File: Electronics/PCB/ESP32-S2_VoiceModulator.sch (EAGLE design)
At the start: 17 parts, among them IC1 ESP32-S2, IC2 AT25SF041-SSHD-B, J1 0532610671, Y1 FA-20H_40.0000MF15Z-AC3

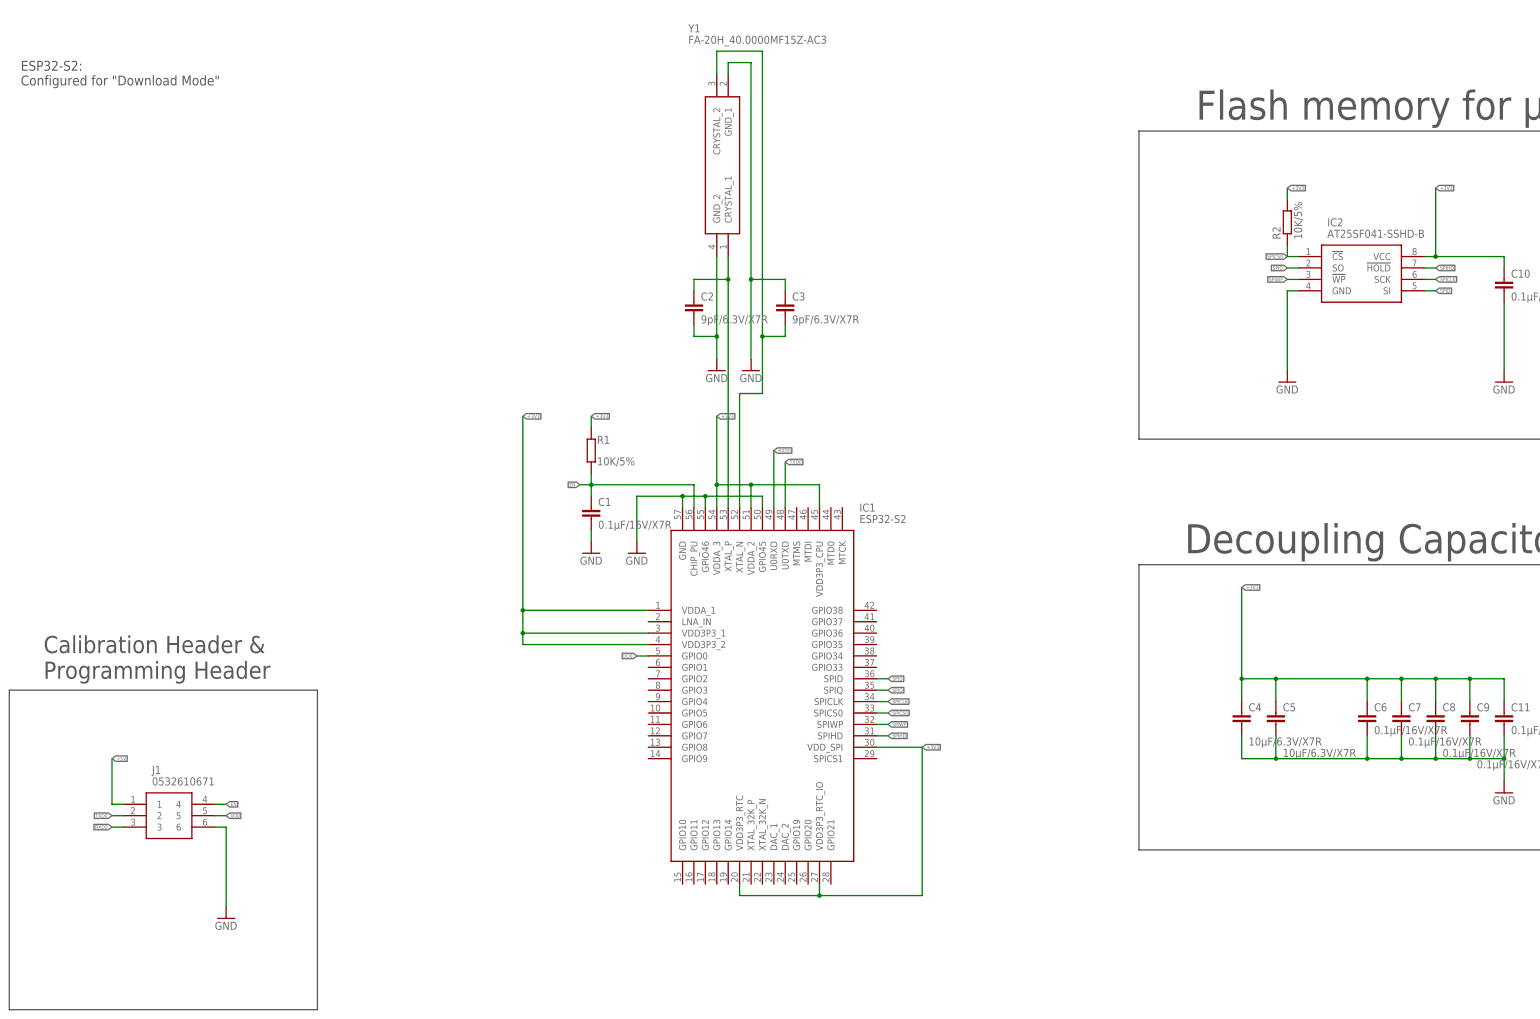
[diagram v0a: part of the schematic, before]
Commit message: CHanged labelign for VCC/ power
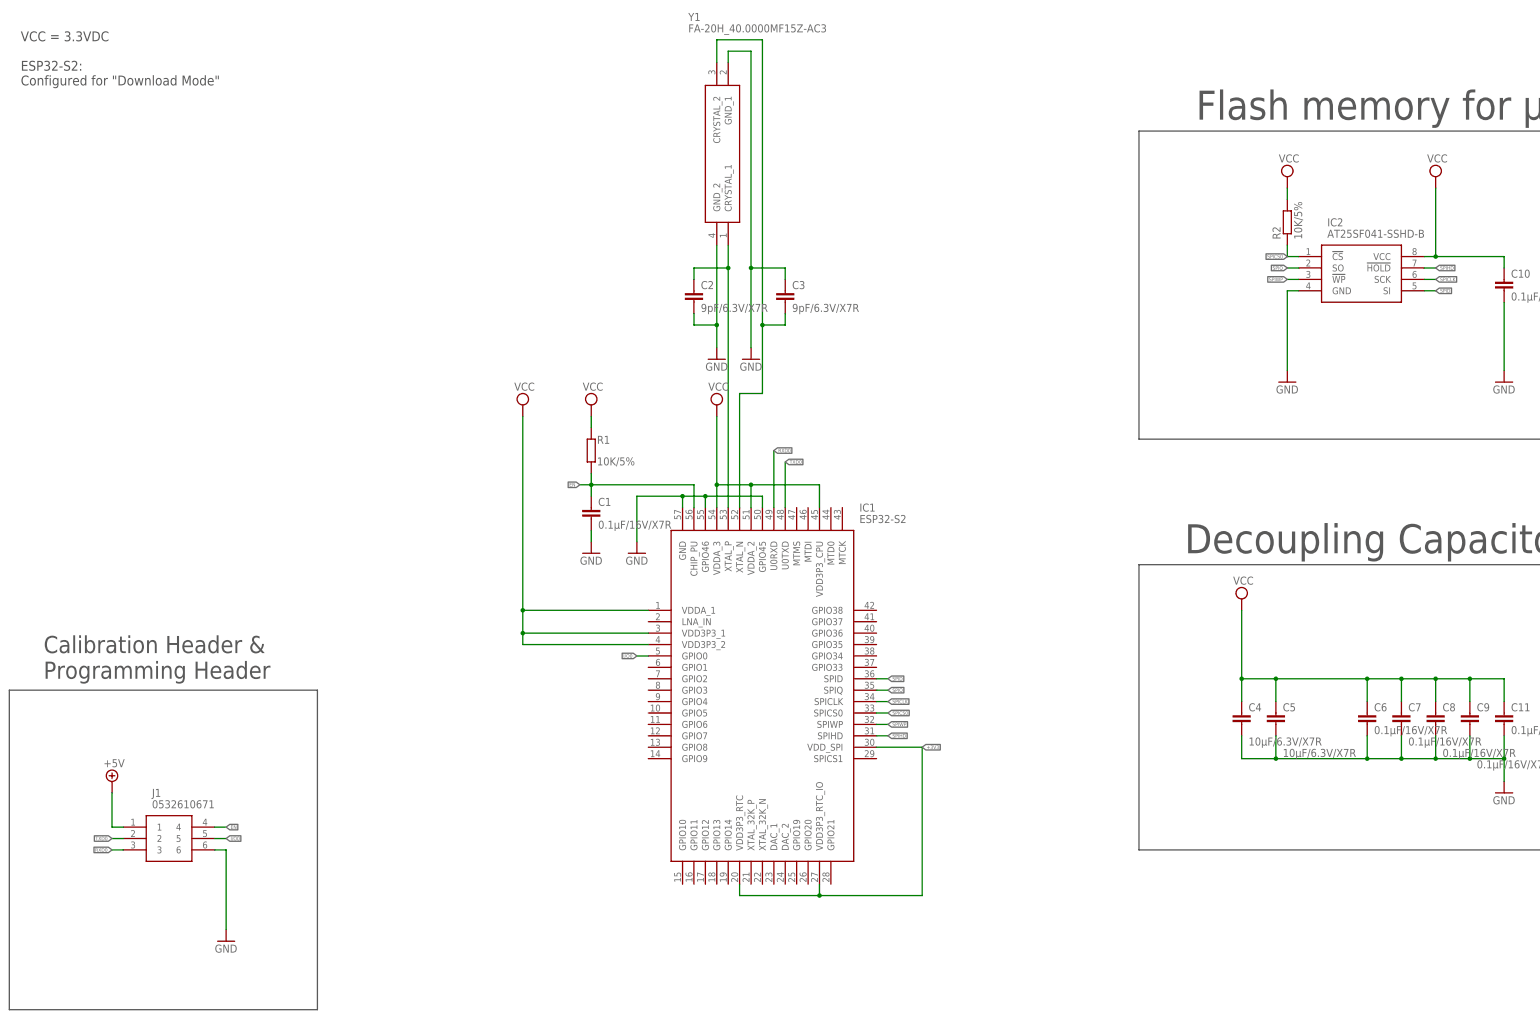
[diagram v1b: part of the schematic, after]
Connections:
- new net VCC: C10.1, C11.1, C4.1, C5.1, C6.1, C7.1, C8.1, C9.1, IC1.VDD3P3_1, IC1.VDD3P3_2, IC1.VDD3P3_CPU, IC1.VDDA_1, IC1.VDDA_2, IC1.VDDA_3, IC2.VCC, R1.2, R2.2
- net +3V3: no longer C10.1, C11.1, C4.1, C5.1, C6.1, C7.1, C8.1, C9.1, IC1.VDD3P3_1, IC1.VDD3P3_2, IC1.VDD3P3_CPU, IC1.VDDA_1, IC1.VDDA_2, IC1.VDDA_3, IC2.VCC, R1.2, R2.2
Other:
- note added: "VCC = 3.3VDC ESP32-S2: Configured for "Download Mode""
- note removed: "ESP32-S2: Configured for "Download Mode""
- moved on the sheet: C2, C3, J1, Y1

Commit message: Added schematic drawing for the microphone emulation and PCB microphone adjustment.
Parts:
- added C12, C13, C15: 1uF/6.3V, resistor:C-EUC0603
- added C14: 0.1µF/16V, rcl:C-EUC0402
- added J2, J3: (no value), VoiceModulator:SJ2-35364B-SMT-TR
- added MK1: WMM7022AT0, VoiceModulator:WMM7022AT0
- added OP1: MCP6001T-I/OT, VoiceModulator:MCP6001T-I/OT
- added Q1: CPH3910, VoiceModulator:CPH3910
- added R10, R9: 1K, resistor:R-EU_R0603
- added R11: 70k, resistor:R-EU_R0603
- added R12, R13, R8: 100K, resistor:R-EU_R0603
- added R3, R5, R6, R7: 10K, resistor:R-EU_R0603
- added R4: 100R, resistor:R-EU_R0603
- C1, C10, C11, C6, C7, C8, C9: value 0.1µF/16V/X7R -> 0.1µF/16V
- C2, C3: value 9pF/6.3V/X7R -> 9pF/6.3V
- C4, C5: value 10µF/6.3V/X7R -> 10µF/6.3V
- R1, R2: value 10K/5% -> 10K
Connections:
- new net AGND: J2.4, J3.4, Q1.S, R5.2
- new net AUDIO_LEFT: J2.2, J3.2
- new net AUDIO_RIGHT: J2.3, J3.3
- new net DAC_OUTPUT: R3.2
- new net HEADPHONE_SWITCH: J2.10
- new net MICROPHONE_HEADSET: J2.1
- new net MICROPHONE_OUT: J3.1, R6.1, R7.2
- new net N$1: C12.2, Q1.G, R5.1
- new net N$2: C12.1, R3.1, R4.2
- new net N$3: C13.2, OP1.V+, R8.1, R9.2
- new net N$4: C13.1, MK1.OUT
- new net N$5: Q1.D, R6.2, R7.1
- new net N$6: OP1.V-, R10.2, R11.2
- new net N$7: C15.1, OP1.VOUT, R11.1
- new net PCB-MICROPHONE_OUTPUT: C15.2, R12.2, R13.1
- new net PHONE_SWITCH: J3.10
- net +5V: now also OP1.VDD
- net GND: now also C14.2, MK1.GND, OP1.VSS, R10.1, R12.1, R4.1, R9.1
- net VCC: now also C14.1, MK1.VDD, R13.2, R8.2
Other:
- note added: "Check if grounding is correct"
- note added: "Headphones"
- note added: "PCB Microphone adjustment"
- note added: "Phone"

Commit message: Added DC/DC
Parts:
- added C16, C17: 1uF/6.3V, resistor:C-EUC0603
- added IC3: MIC5504-3.3YM5-TR, VoiceModulator:MIC5504-3.3YM5-TR
- J2, J3: value (none) -> SJ2-35364B-SMT-TR
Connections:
- net +5V: now also C16.1, IC3.EN, IC3.VIN
- net GND: now also C16.2, C17.2, IC3.GND
- net VCC: now also C17.1, IC3.VOUT
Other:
- note added: "<--- So lonely in a vast empty space :("
- note added: "Microphone emulation"
- note added: "ToDo: Replace ESP32-S2 symbol with functional pinout"

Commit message: Minor changes to schematic
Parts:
- removed J1: 0532610671, SamacSys_Parts:0532610671
- added C18: 0.1µF/16V, resistor:C-EUC0603
- added C19: 0.1µF/16V, rcl:C-EUC0402
- added C20: 1uF/6.3V, resistor:C-EUC0603
- added C21: 10µF/6.3V, rcl:C-EUC0603
- added J4: 10118192-0002LF, VoiceModulator:10118192-0002LF
- added OP2: MCP6001T-I/OT, VoiceModulator:MCP6001T-I/OT
- added R14, R18, R19, R20: 100K, resistor:R-EU_R0603
- added R15, R16: 1K, resistor:R-EU_R0603
- added R17: 70k, resistor:R-EU_R0603
- added TAG_CONNECT_ICSP_HEADER: TAG-CONNECT_PADS, TAG-CONNECT_PADS-lbr:TAG-CONNECT_PADS
- J2: SPICEPREFIX (none) -> X
- R3: value 10K -> 100K
- R4: value 100R -> 1k
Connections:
- removed net AGND: J2.4, J3.4, Q1.S, R5.2
- new net D+: IC1.GPIO19, J4.3
- new net D-: IC1.GPIO20, J4.2
- new net EXTERNAL-MICROPHONE_OUTPUT: C20.2, R18.2, R19.1
- new net ID: J4.4
- new net N$10: OP2.V-, R16.2, R17.2
- new net N$11: C20.1, OP2.VOUT, R17.1
- new net N$9: C18.2, OP2.V+, R14.1, R15.2
- net +5V: now also C21.1, J4.1, OP2.VDD, TAG_CONNECT_ICSP_HEADER.MISO; no longer J1.1
- net EN: now also TAG_CONNECT_ICSP_HEADER.VCC; no longer J1.4
- net GND: now also C19.2, C21.2, J2.4, J3.4, J4.5, OP2.VSS, Q1.S, R15.1, R16.1, R18.1, R5.2, TAG_CONNECT_ICSP_HEADER.GND; no longer J1.6
- net I/O0: now also TAG_CONNECT_ICSP_HEADER.MOSI; no longer J1.5
- net MICROPHONE_HEADSET: now also C18.1, C19.1, R20.1
- net RXD0: now also TAG_CONNECT_ICSP_HEADER.RST; no longer J1.3
- net TXD0: now also TAG_CONNECT_ICSP_HEADER.SCK; no longer J1.2
- net VCC: now also R14.2, R19.2, R20.2
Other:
- note added: "External Microphone adjustment"
- note removed: "Check if grounding is correct"

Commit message: Minor changes
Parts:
- added R21, R22, R23, R24: 10K, resistor:R-EU_R0603
- added S1, S2, S3, S4: PTS647SK70SMTR2LFS, VoiceModulator:PTS647SK70SMTR2LFS
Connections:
- new net SW_1: R21.2, S1.2
- new net SW_2: R22.2, S2.2
- new net SW_3: R23.2, S3.2
- new net SW_4: R24.2, S4.2
- net GND: now also S1.1, S2.1, S3.1, S4.1
- net VCC: now also R21.1, R22.1, R23.1, R24.1
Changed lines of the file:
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@@
 <part name="GND21" library="supply1" library_urn="urn:adsk.eagle:library:371" deviceset="GND" device=""/>
 <part name="GND22" library="supply1" library_urn="urn:adsk.eagle:library:371" deviceset="GND" device=""/>
+<part name="FRAME3" library="frames" library_urn="urn:adsk.eagle:library:229" deviceset="A4L-LOC" device=""/>
+<part name="S1" library="VoiceModulator" deviceset="PTS647SK70SMTR2LFS" device="" override_package3d_urn="urn:adsk.eagle:package:24950186/2" override_package_urn="urn:adsk.eagle:footprint:24950187/1"/>
+<part name="S2" library="VoiceModulator" deviceset="PTS647SK70SMTR2LFS" device="" override_package3d_urn="urn:adsk.eagle:package:24950189/2" override_package_urn="urn:adsk.eagle:footprint:24950190/1"/>
+<part name="S3" library="VoiceModulator" deviceset="PTS647SK70SMTR2LFS" device="" override_package3d_urn="urn:adsk.eagle:package:24950193/2" override_package_urn="urn:adsk.eagle:footprint:24950194/1"/>
+<part name="S4" library="VoiceModulator" deviceset="PTS647SK70SMTR2LFS" device="" override_package3d_urn="urn:adsk.eagle:package:24950197/2" override_package_urn="urn:adsk.eagle:footprint:24950198/1"/>
+<part name="GND23" library="supply1" library_urn="urn:adsk.eagle:library:371" deviceset="GND" device=""/>
+<part name="R21" library="resistor" library_urn="urn:adsk.eagle:library:348" deviceset="R-EU_" device="R0603" package3d_urn="urn:adsk.eagle:package:23555/3" value="10K"/>
+<part name="R22" library="resistor" library_urn="urn:adsk.eagle:library:348" deviceset="R-EU_" device="R0603" package3d_urn="urn:adsk.eagle:package:23555/3" value="10K"/>
+<part name="R23" library="resistor" library_urn="urn:adsk.eagle:library:348" deviceset="R-EU_" device="R0603" package3d_urn="urn:adsk.eagle:package:23555/3" value="10K"/>
+<part name="R24" library="resistor" library_urn="urn:adsk.eagle:library:348" deviceset="R-EU_" device="R0603" package3d_urn="urn:adsk.eagle:package:23555/3" value="10K"/>
+<part name="SUPPLY7" library="supply2" library_urn="urn:adsk.eagle:library:372" deviceset="VCC" device=""/>
 </parts>
 <sheets>
@@
 <attribute name="VALUE" x="137.16" y="106.68" size="1.6764" layer="96"/>
 </instance>
-<instance part="GND13" gate="1" x="73.66" y="76.2" smashed="yes">
-<attribute name="VALUE" x="71.12" y="73.66" size="1.778" layer="96"/>
+<instance part="GND13" gate="1" x="73.66" y="73.66" smashed="yes">
+<attribute name="VALUE" x="71.12" y="71.12" size="1.778" layer="96"/>
 </instance>
 <instance part="C21" gate="G$1" x="91.44" y="91.44" smashed="yes">
@@
 <attribute name="VALUE" x="95.504" y="89.281" size="1.778" layer="96"/>
 </instance>
-<instance part="GND18" gate="1" x="91.44" y="76.2" smashed="yes">
-<attribute name="VALUE" x="88.9" y="73.66" size="1.778" layer="96"/>
+<instance part="GND18" gate="1" x="91.44" y="73.66" smashed="yes">
+<attribute name="VALUE" x="88.9" y="71.12" size="1.778" layer="96"/>
 </instance>
 <instance part="FRAME5" gate="G$1" x="0" y="0" smashed="yes">
@@
 <segment>
 <wire x1="71.12" y1="88.9" x2="73.66" y2="88.9" width="0.1524" layer="91"/>
-<wire x1="73.66" y1="88.9" x2="73.66" y2="78.74" width="0.1524" layer="91"/>
+<wire x1="73.66" y1="88.9" x2="73.66" y2="76.2" width="0.1524" layer="91"/>
 <pinref part="GND13" gate="1" pin="GND"/>
 <pinref part="J4" gate="A" pin="5"/>
@@
 <segment>
 <pinref part="C21" gate="G$1" pin="2"/>
-<wire x1="91.44" y1="86.36" x2="91.44" y2="78.74" width="0.1524" layer="91"/>
+<wire x1="91.44" y1="86.36" x2="91.44" y2="76.2" width="0.1524" layer="91"/>
 <pinref part="GND18" gate="1" pin="GND"/>
 </segment>
@@
 </segment>
 </net>
+</nets>
+</sheet>
+<sheet>
+<description>Buttons</description>
+<plain>
+</plain>
+<instances>
+<instance part="FRAME3" gate="G$1" x="0" y="0" smashed="yes">
+<attribute name="DRAWING_NAME" x="217.17" y="15.24" size="2.54" layer="94"/>
+<attribute name="LAST_DATE_TIME" x="217.17" y="10.16" size="2.286" layer="94"/>
+<attribute name="SHEET" x="230.505" y="5.08" size="2.54" layer="94"/>
+</instance>
+<instance part="S1" gate="G$1" x="58.42" y="119.38" smashed="yes">
+<attribute name="NAME" x="50.8" y="124.46" size="1.778" layer="95"/>
+</instance>
+<instance part="S2" gate="G$1" x="58.42" y="106.68" smashed="yes">
+<attribute name="NAME" x="50.8" y="111.76" size="1.778" layer="95"/>
+</instance>
+<instance part="S3" gate="G$1" x="58.42" y="93.98" smashed="yes">
+<attribute name="NAME" x="50.8" y="99.06" size="1.778" layer="95"/>
+</instance>
+<instance part="S4" gate="G$1" x="58.42" y="81.28" smashed="yes">
+<attribute name="NAME" x="50.8" y="86.36" size="1.778" layer="95"/>
+</instance>
+<instance part="GND23" gate="1" x="43.18" y="55.88" smashed="yes">
+<attribute name="VALUE" x="40.64" y="53.34" size="1.778" layer="96"/>
+</instance>
+<instance part="R21" gate="G$1" x="81.28" y="132.08" smashed="yes" rot="R270">
+<attribute name="NAME" x="82.55" y="131.0386" size="1.778" layer="95"/>
+<attribute name="VALUE" x="82.55" y="128.778" size="1.778" layer="96"/>
+</instance>
+<instance part="R22" gate="G$1" x="88.9" y="132.08" smashed="yes" rot="R270">
+<attribute name="NAME" x="90.17" y="131.0386" size="1.778" layer="95"/>
+<attribute name="VALUE" x="90.17" y="128.778" size="1.778" layer="96"/>
+</instance>
+<instance part="R23" gate="G$1" x="99.06" y="132.08" smashed="yes" rot="R270">
+<attribute name="NAME" x="100.33" y="131.0386" size="1.778" layer="95"/>
+<attribute name="VALUE" x="100.33" y="128.778" size="1.778" layer="96"/>
+</instance>
+<instance part="R24" gate="G$1" x="106.68" y="132.08" smashed="yes" rot="R270">
+<attribute name="NAME" x="107.95" y="131.0386" size="1.778" layer="95"/>
+<attribute name="VALUE" x="107.95" y="128.778" size="1.778" layer="96"/>
+</instance>
+<instance part="SUPPLY7" gate="G$1" x="93.98" y="154.94" smashed="yes">
+<attribute name="VALUE" x="92.075" y="158.115" size="1.778" layer="96"/>
+</instance>
+</instances>
+<busses>
+</busses>
+<nets>
+<net name="GND" class="0">
+<segment>
+<pinref part="S4" gate="G$1" pin="1"/>
+<pinref part="GND23" gate="1" pin="GND"/>
+<wire x1="48.26" y1="81.28" x2="43.18" y2="81.28" width="0.1524" layer="91"/>
+<wire x1="43.18" y1="81.28" x2="43.18" y2="58.42" width="0.1524" layer="91"/>
+<pinref part="S3" gate="G$1" pin="1"/>
+<wire x1="48.26" y1="93.98" x2="43.18" y2="93.98" width="0.1524" layer="91"/>
+<wire x1="43.18" y1="93.98" x2="43.18" y2="81.28" width="0.1524" layer="91"/>
+<junction x="43.18" y="81.28"/>
+<pinref part="S2" gate="G$1" pin="1"/>
+<wire x1="48.26" y1="106.68" x2="43.18" y2="106.68" width="0.1524" layer="91"/>
+<wire x1="43.18" y1="106.68" x2="43.18" y2="93.98" width="0.1524" layer="91"/>
+<junction x="43.18" y="93.98"/>
+<pinref part="S1" gate="G$1" pin="1"/>
+<wire x1="48.26" y1="119.38" x2="43.18" y2="119.38" width="0.1524" layer="91"/>
+<wire x1="43.18" y1="119.38" x2="43.18" y2="106.68" width="0.1524" layer="91"/>
+<junction x="43.18" y="106.68"/>
+</segment>
+</net>
+<net name="SW_1" class="0">
+<segment>
+<pinref part="S1" gate="G$1" pin="2"/>
+<pinref part="R21" gate="G$1" pin="2"/>
+<wire x1="81.28" y1="127" x2="81.28" y2="119.38" width="0.1524" layer="91"/>
+<wire x1="81.28" y1="119.38" x2="68.58" y2="119.38" width="0.1524" layer="91"/>
+<label x="81.28" y="119.38" size="0.8128" layer="95" xref="yes"/>
+</segment>
+</net>
+<net name="SW_2" class="0">
+<segment>
+<pinref part="R22" gate="G$1" pin="2"/>
+<pinref part="S2" gate="G$1" pin="2"/>
+<wire x1="88.9" y1="127" x2="88.9" y2="106.68" width="0.1524" layer="91"/>
+<wire x1="88.9" y1="106.68" x2="68.58" y2="106.68" width="0.1524" layer="91"/>
+<label x="88.9" y="106.68" size="0.8128" layer="95" xref="yes"/>
+</segment>
+</net>
+<net name="SW_3" class="0">
+<segment>
+<pinref part="R23" gate="G$1" pin="2"/>
+<pinref part="S3" gate="G$1" pin="2"/>
+<wire x1="99.06" y1="127" x2="99.06" y2="93.98" width="0.1524" layer="91"/>
+<wire x1="99.06" y1="93.98" x2="68.58" y2="93.98" width="0.1524" layer="91"/>
+<label x="99.06" y="93.98" size="0.8128" layer="95" xref="yes"/>
+</segment>
+</net>
+<net name="SW_4" class="0">
+<segment>
+<pinref part="R24" gate="G$1" pin="2"/>
+<pinref part="S4" gate="G$1" pin="2"/>
+<wire x1="106.68" y1="127" x2="106.68" y2="81.28" width="0.1524" layer="91"/>
+<wire x1="106.68" y1="81.28" x2="68.58" y2="81.28" width="0.1524" layer="91"/>
+<label x="106.68" y="81.28" size="0.8128" layer="95" xref="yes"/>
+</segment>
+</net>
+<net name="VCC" class="0">
+<segment>
+<pinref part="R21" gate="G$1" pin="1"/>
+<wire x1="81.28" y1="137.16" x2="81.28" y2="139.7" width="0.1524" layer="91"/>
+<wire x1="81.28" y1="139.7" x2="88.9" y2="139.7" width="0.1524" layer="91"/>
+<pinref part="R22" gate="G$1" pin="1"/>
+<wire x1="88.9" y1="139.7" x2="88.9" y2="137.16" width="0.1524" layer="91"/>
+<pinref part="R23" gate="G$1" pin="1"/>
+<wire x1="99.06" y1="137.16" x2="99.06" y2="139.7" width="0.1524" layer="91"/>
+<wire x1="99.06" y1="139.7" x2="93.98" y2="139.7" width="0.1524" layer="91"/>
+<junction x="88.9" y="139.7"/>
+<pinref part="R24" gate="G$1" pin="1"/>
+<wire x1="93.98" y1="139.7" x2="88.9" y2="139.7" width="0.1524" layer="91"/>
+<wire x1="106.68" y1="137.16" x2="106.68" y2="139.7" width="0.1524" layer="91"/>
+<wire x1="106.68" y1="139.7" x2="99.06" y2="139.7" width="0.1524" layer="91"/>
+<junction x="99.06" y="139.7"/>
+<pinref part="SUPPLY7" gate="G$1" pin="VCC"/>
+<wire x1="93.98" y1="152.4" x2="93.98" y2="139.7" width="0.1524" layer="91"/>
+<junction x="93.98" y="139.7"/>
+</segment>
+</net>
